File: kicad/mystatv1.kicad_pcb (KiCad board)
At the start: 2 copper layers, 55.5 x 65 mm, 66 parts, among them K1 9007-05-01, K2 9007-05-01, K3 9007-05-01, K4 9007-05-01, P1 USB Terminal, P2 CELL, P3 ICSP, U1 LM2662, U2 PIC16F1459, U3 ADR421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

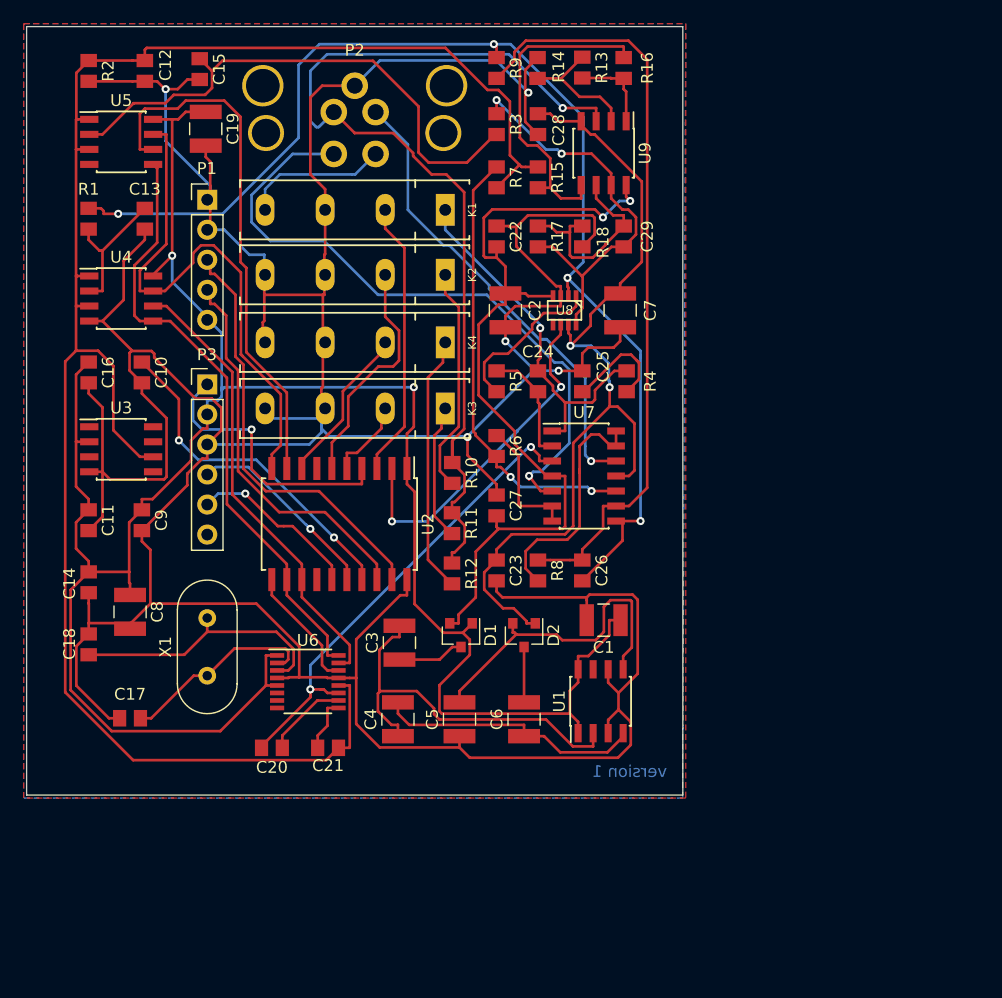
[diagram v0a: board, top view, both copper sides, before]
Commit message: Add files via upload
Changed layout.  Added guard ring for the DAC1220.  Used wider traces.  Manually routed everything.
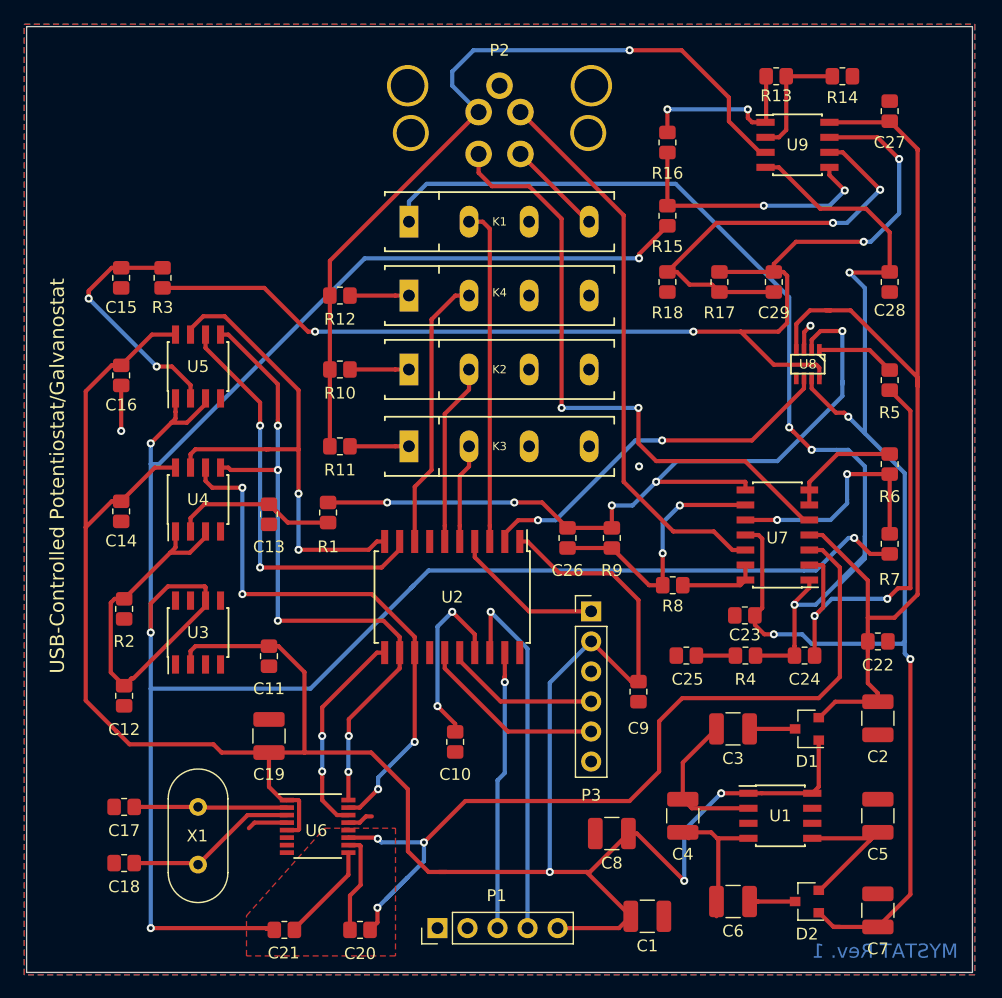
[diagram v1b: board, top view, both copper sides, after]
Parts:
- moved P1 64.6 mm to (84.8, 126.2), turned to 90 degrees
- moved C7 55.2 mm to (122.0, 124.8), turned to 270 degrees
- moved C12 52.9 mm to (58.2, 106.6)
- moved C19 51.6 mm to (70.5, 110.0), turned to 90 degrees
- moved C27 47.1 mm to (123.0, 57.1)
- moved C22 47.0 mm to (122.0, 102.0), turned to 180 degrees
- moved C2 46.7 mm to (122.0, 108.5)
- moved R2 45.6 mm to (58.2, 99.2)
- moved R7 45.5 mm to (123.0, 93.8)
- moved C8 44.9 mm to (99.5, 118.2), turned to 180 degrees
- moved C9 44.4 mm to (101.8, 106.2)
- moved C10 41.0 mm to (86.2, 110.5)
- moved R9 40.9 mm to (99.5, 93.2)
- moved P3 37.7 mm to (97.8, 99.5)
- moved C5 36.3 mm to (122.0, 116.8), turned to 270 degrees
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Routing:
- net GND: track 381.4 -> 11.7 mm, vias 5 -> 3
- net /VREF: track 153.7 -> 220.4 mm, vias 0 -> 5
- net /I_MEAS: track 35.1 -> 97.6 mm, vias 2 -> 4
- net Net-(C24-Pad1): track 30.9 -> 87.7 mm, vias 1 -> 3
- net Net-(C26-Pad1): track 64.8 -> 22.2 mm, vias 0 -> 2
- net -9V: track 74.1 -> 113.6 mm, vias 2 -> 4
- net /V_MEAS: track 103.6 -> 67.9 mm, vias 4 -> 5
- net Net-(C20-Pad2): track 40.5 -> 74.2 mm, vias 2 -> 3
- net +5V: track 185.6 -> 215.6 mm, vias 2 -> 3
- net Net-(C24-Pad2): track 9.96 -> 35.6 mm, vias 0 -> 2
- net Net-(C15-Pad1): track 46.2 -> 20.5 mm, vias 0 -> 2
- net +9V: track 69.9 -> 90.3 mm, vias 2 -> 0
- net Net-(C3-Pad2): track 32.9 -> 13.0 mm
- net Net-(C29-Pad1): track 17.1 -> 36.2 mm, vias 0 -> 2
- net Net-(R6-Pad2): track 38.0 -> 20.3 mm
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- added copper zone on F.Cu, net /VREF
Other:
- board size 55.5 x 65 mm -> 80 x 80 mm
- net class power added: clearance 0.2286, trace_width 0.2286, via_dia 0.6858, via_drill 0.3302
- board text added: "MYSTAT Rev. 1"
- board text added: "USB-Controlled Potentiostat/Galvanostat"
- board text removed: "version 1"
